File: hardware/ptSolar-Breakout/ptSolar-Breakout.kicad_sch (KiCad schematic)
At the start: 3 parts, among them J1 6 Pin Male Header, J2 Qwiic, J3 6 Pin Male Header

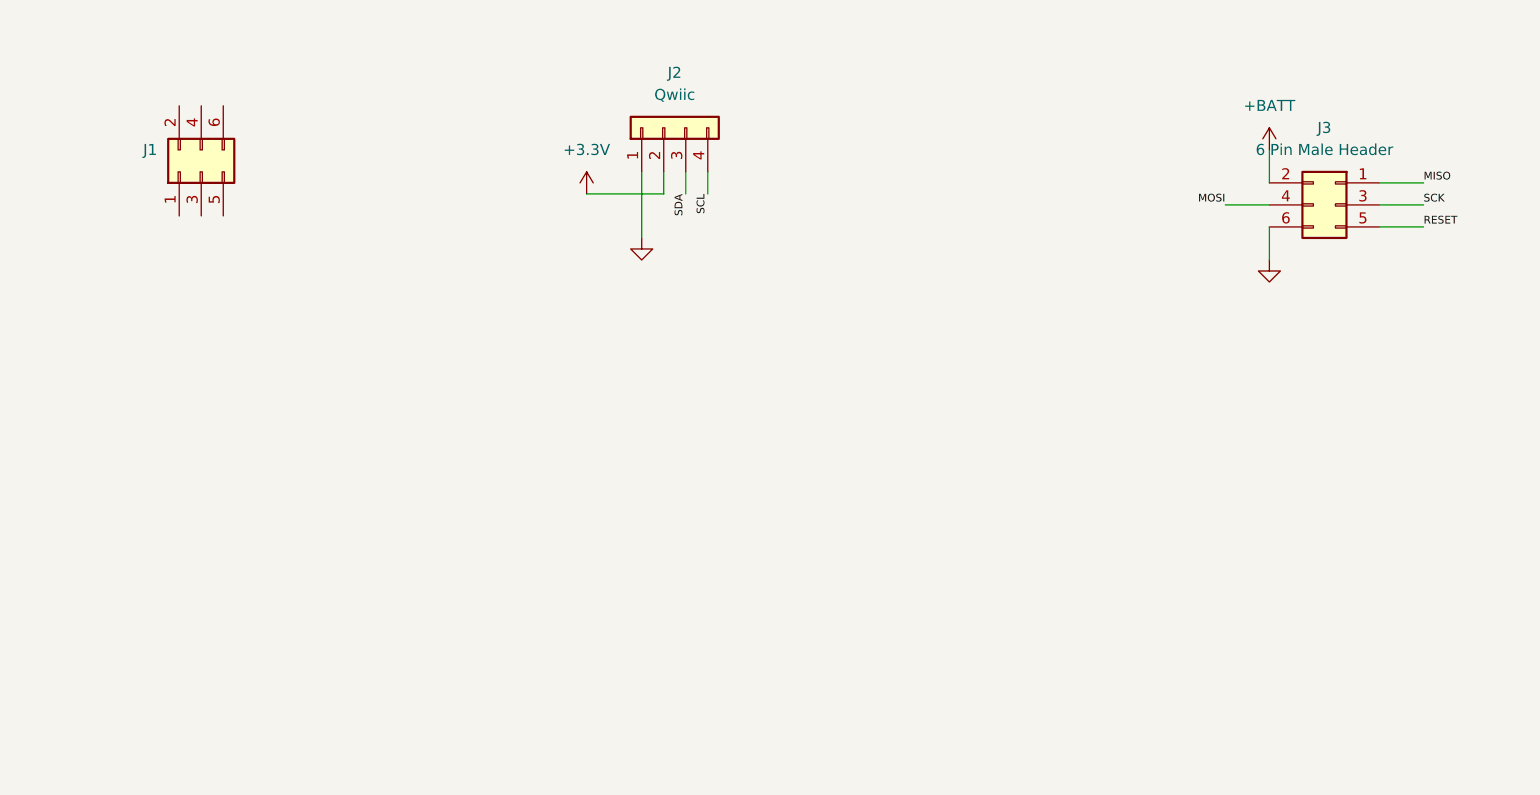
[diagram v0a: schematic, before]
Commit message: Added Breakout Board for powering and programming the ptSolar.
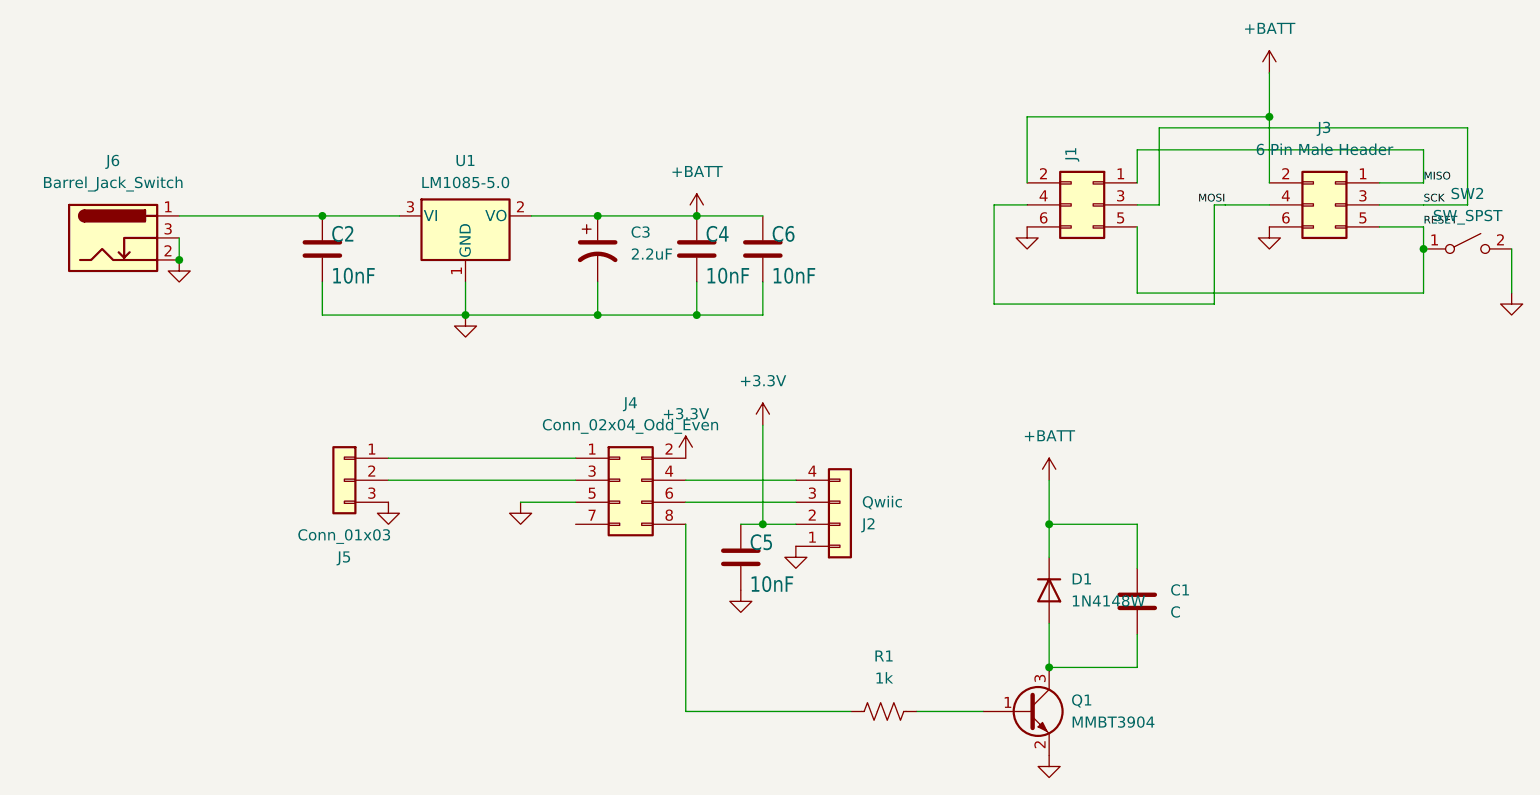
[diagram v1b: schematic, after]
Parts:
- added C1: C, Capacitor_THT:CP_Radial_D12.5mm_P7.50mm, symbol Device:C
- added C2, C4, C5, C6: 10nF, Capacitor_SMD:C_0805_2012Metric, symbol Device:C
- added C3: 2.2uF, Capacitor_SMD:C_0805_2012Metric, symbol Device:C_Polarized_US
- added D1: 1N4148W, Diode_SMD:D_SOD-123, symbol Diode:1N4148W
- added J4: Conn_02x04_Odd_Even, Connector_PinHeader_2.54mm:PinHeader_2x04_P2.54mm_Vertical, symbol Connector_Generic:Conn_02x04_Odd_Even
- added J5: Conn_01x03, Connector_PinHeader_2.54mm:PinHeader_1x03_P2.54mm_Vertical, symbol Connector_Generic:Conn_01x03
- added J6: Barrel_Jack_Switch, Connector_BarrelJack:BarrelJack_CLIFF_FC681465S_SMT_Horizontal, symbol Connector:Barrel_Jack_Switch
- added Q1: MMBT3904, Package_TO_SOT_SMD:SOT-23, symbol Transistor_BJT:MMBT3904
- added R1: 1k, Resistor_SMD:R_0805_2012Metric, symbol Device:R_US
- added SW2: SW_SPST, Button_Switch_SMD:SW_SPST_B3S-1000, symbol Switch:SW_SPST
- added U1: LM1085-5.0, Package_TO_SOT_SMD:TO-263-3_TabPin2, symbol Regulator_Linear:LM1085-5.0
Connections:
- net +3.3V: now also C5.1, J4.2 (Pin_2)
- net +BATT: now also J1.2 (Pin_2), C1.1, C3.1, C4.1, C6.1, D1.1 (K), U1.2 (VO)
- net GND: now also J1.6 (Pin_6), C2.2, C3.2, C4.2, C5.2, C6.2, J4.5 (Pin_5), J5.3 (Pin_3), J6.2, J6.3, Q1.2 (E), SW2.2 (B), U1.1 (GND)
- net MISO: now also J1.1 (Pin_1)
- net MOSI: now also J1.4 (Pin_4)
- net RESET: now also J1.5 (Pin_5), SW2.1 (A)
- net SCK: now also J1.3 (Pin_3)
- net SCL: no longer names the net of J2.4 (Pin_4)
- net SCL: now also J4.4 (Pin_4)
- net SDA: no longer names the net of J2.3 (Pin_3)
- net SDA: now also J4.6 (Pin_6)
- new net: C2.1, J6.1, U1.3 (VI)
- new net: J4.1 (Pin_1), J5.1 (Pin_1)
- new net: J4.3 (Pin_3), J5.2 (Pin_2)
- new net: Q1.1 (B), R1.2
- new net: C1.2, D1.2 (A), Q1.3 (C)
- new net: J4.8 (Pin_8), R1.1
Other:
- moved on the sheet: J1
